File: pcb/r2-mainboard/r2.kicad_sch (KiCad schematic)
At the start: 0 parts

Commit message: R2: the six approved edits, and one of them was already done
Owner-approved 2026-08-19, KiCad closed for the pass.

1. R225 22k -> 20.5K/1%, LCSC C57105 (0402WGF2052TCE, UNI-ROYAL, the
   family the rest of the board already uses). Rendered and checked:
   R224 390k over R225 20.5k with R213 100k injecting VGH_DAC, so
   20.5||100 = 17.01k and VGH = 1.2 x (1 + 390/17.01) = 28.71 V at
   DAC = 0 -- exactly epd-port.md 10.3's target.
2. The five sense-divider caps that carried codes for the wrong
   capacitance -> C1523 (0402B102K500NT, 1 nF 50 V X7R, JLC Basic,
   5.3 M stock). One part covers both the 25 V and 50 V positions.
2b. R88/R224 -> C54920667 (HRC0402F3903DNTO, 390k 1%, 20 k stock).
   C25782 had 14 units against two per board. The owner found this one;
   both obvious alternatives were traps -- C23150 is 0603, and C44937
   is 3.9 ohm despite "390K" in its part number.
3. C147 set DNP rather than deleted. panel.md 7 had already ruled that
   J6.7/J6.44 stay; that covered the pins but not the capacitor on the
   dead net. DNP drops it from placement, keeps the topology of a frozen
   sheet untouched, and leaves the footprint if a future panel drives
   the rail. in_bom stays yes -- that is this board's convention for all
   13 DNP parts, so they show up flagged rather than vanishing.
4. Ten duplicate #PWR references renumbered to #PWR1112-1121 on the
   battery sheet, which was the colliding side in every case.
5. J3 was already deleted on 2026-08-15. No work needed.
6. Specter -> Reflow across 22 files: 14 sheets, 7 generators, the
   project file. .history/ deliberately untouched.

Verified as one change: netlist before and after has 518 nets with
identical pin membership, and epd_power and epd were rendered to PNG and
inspected.

Docs updated to match: epd-port.md 10 is applied rather than designed,
frontlight.md 1 loses the "9 in series is inferred" hedge (the vendor
listing confirms 2 x 9), and io-expansion.md 4's "only guess on this
sheet" is resolved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
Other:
- title: Glider-R2 / Specter mainboard -> Glider-R2 / Reflow mainboard
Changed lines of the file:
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@@
 	(paper "A3")
 	(title_block
-		(title "Glider-R2 / Specter mainboard")
+		(title "Glider-R2 / Reflow mainboard")
 		(date "2026-08-05")
 		(rev "A")

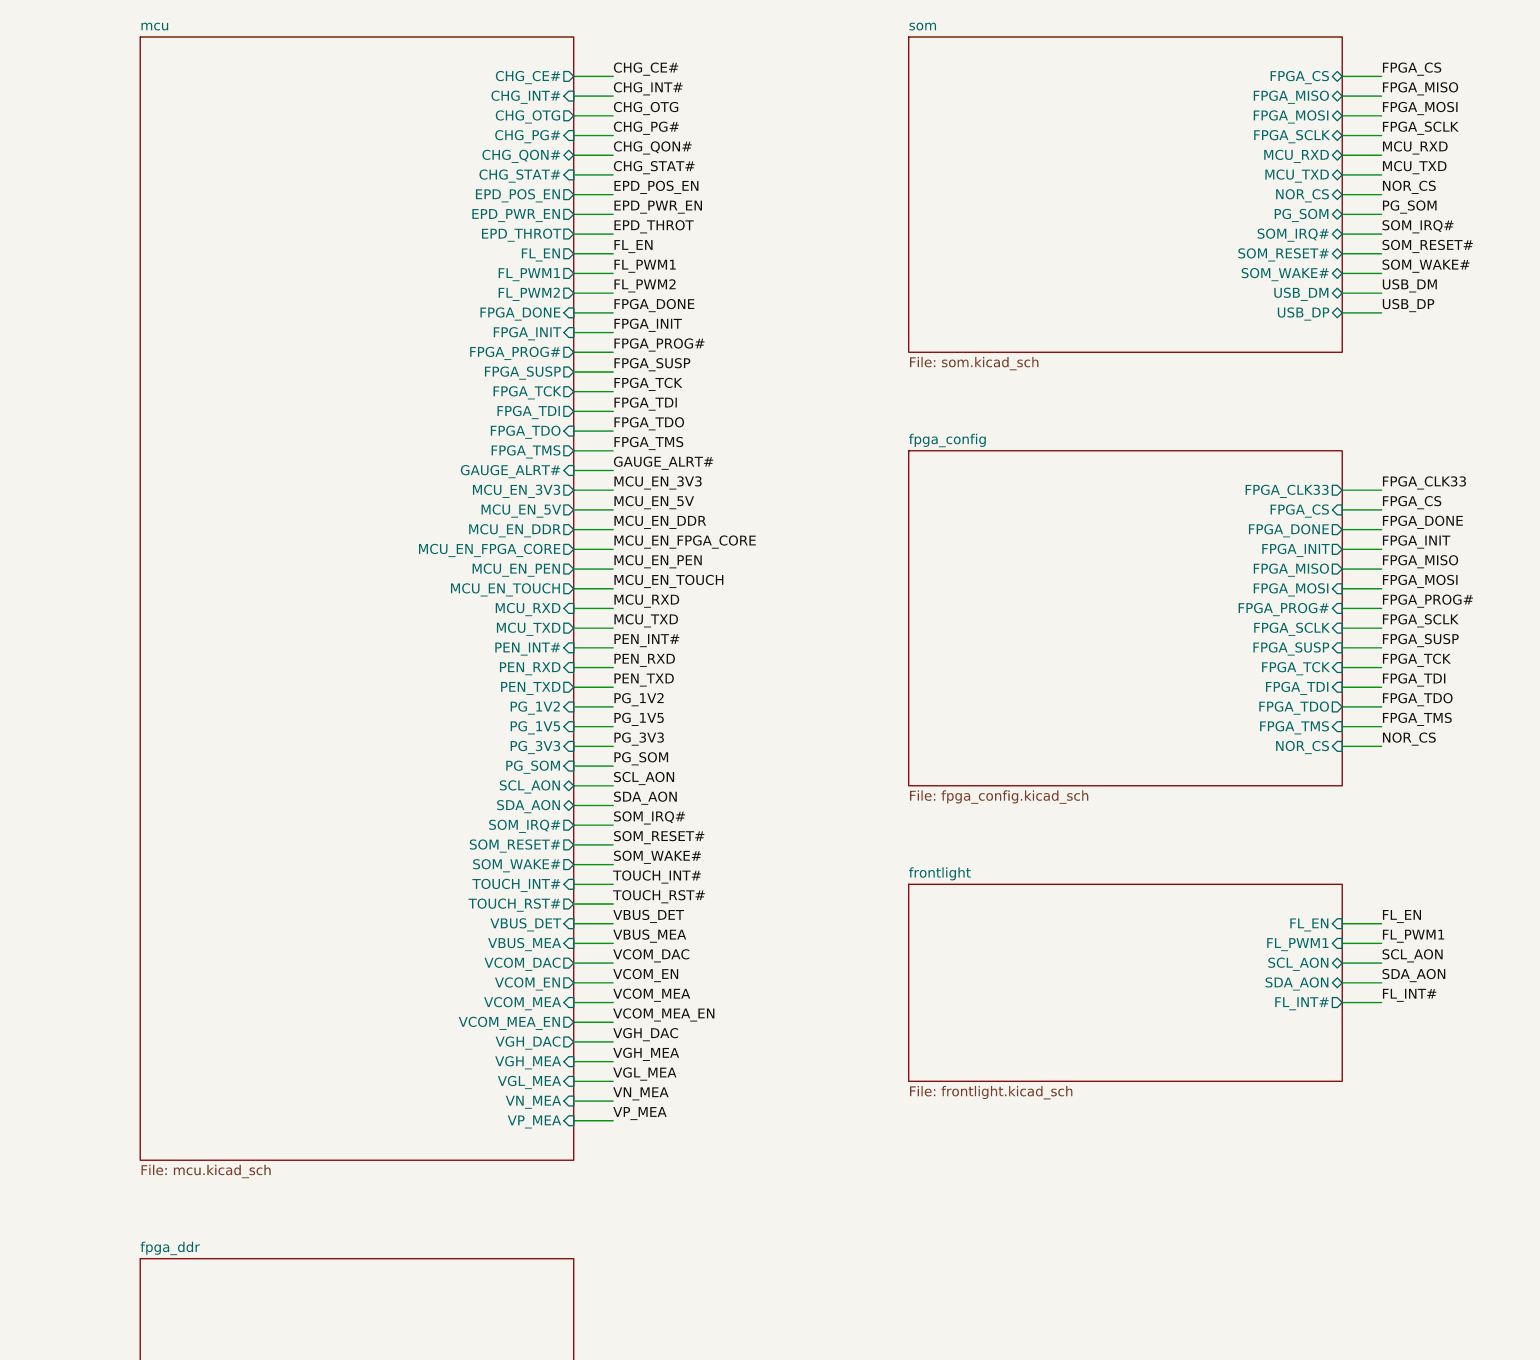
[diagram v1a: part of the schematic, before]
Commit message: R2: the SoM can now reset the MCU and force its bootloader (WP8 closed)
tools/patch_som_mcu_recovery.py applies mcu.md 5.8. On som, A59 and A60
lose their no-connects and gain SOM_MCU_NRST / SOM_MCU_BOOT0. On mcu,
three parts land on empty canvas at x>300:

  Q9    AO3400A  Transistor_FET:Q_NMOS_GSD, SOT-23, C347475
  R510  100k     gate pull-down
  R511  1k       series into PA14

NRST goes through the FET rather than straight to the pin, because the
MCU gates the SoM's own supply -- "SoM off, MCU alive" is the normal
standby state, and a direct tie would let an unpowered A59 clamp
MCU_NRST toward a dead VDDSHV_CANUART and hold the MCU in reset for
good. With Q9 the default is safe in every combination: gate low or SoM
unpowered leaves NRST to the STM32's internal pull-up.

BOOT0 needs no FET -- nothing on R2 drives PA14 high, so R40's pull-down
already defines the safe state, and R511 doubles as the contention limit
against an ST-LINK on the shared SWCLK pin.

Verified: 518 nets before and after; the only membership changes are
MCU_NRST += Q9.3, MCU_SWCLK += R511.2, GND += Q9.2/R510.2, plus the two
new nets and the two unconnected- entries that went away. Rendered to
PNG and inspected twice -- the first layout ran the MCU_NRST label
vertically into the BOOT0 row, so the drain now turns right first.

One trap recorded in mcu.md 5.8: set_sheet_pins re-lays every pin on a
root box, and the root's stubs and labels are positional, so adding two
pins silently rotated the membership of eighteen nets on the first run.
wire_root.py must be re-run after any sheet-pin change; the patch script
now does that itself and asserts on its exit code.

RM0444 (now in datasheets/) settles the factory question from source:
3.3.1 p.67, the EMPTY flag "allows easy programming of virgin devices by
the boot loader", so a blank board needs only an SD card. Riders: the
first flash needs a power cycle or OBL_LAUNCH to reload option bytes,
and the BOOT0 pin still earns its keep for recovery, w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
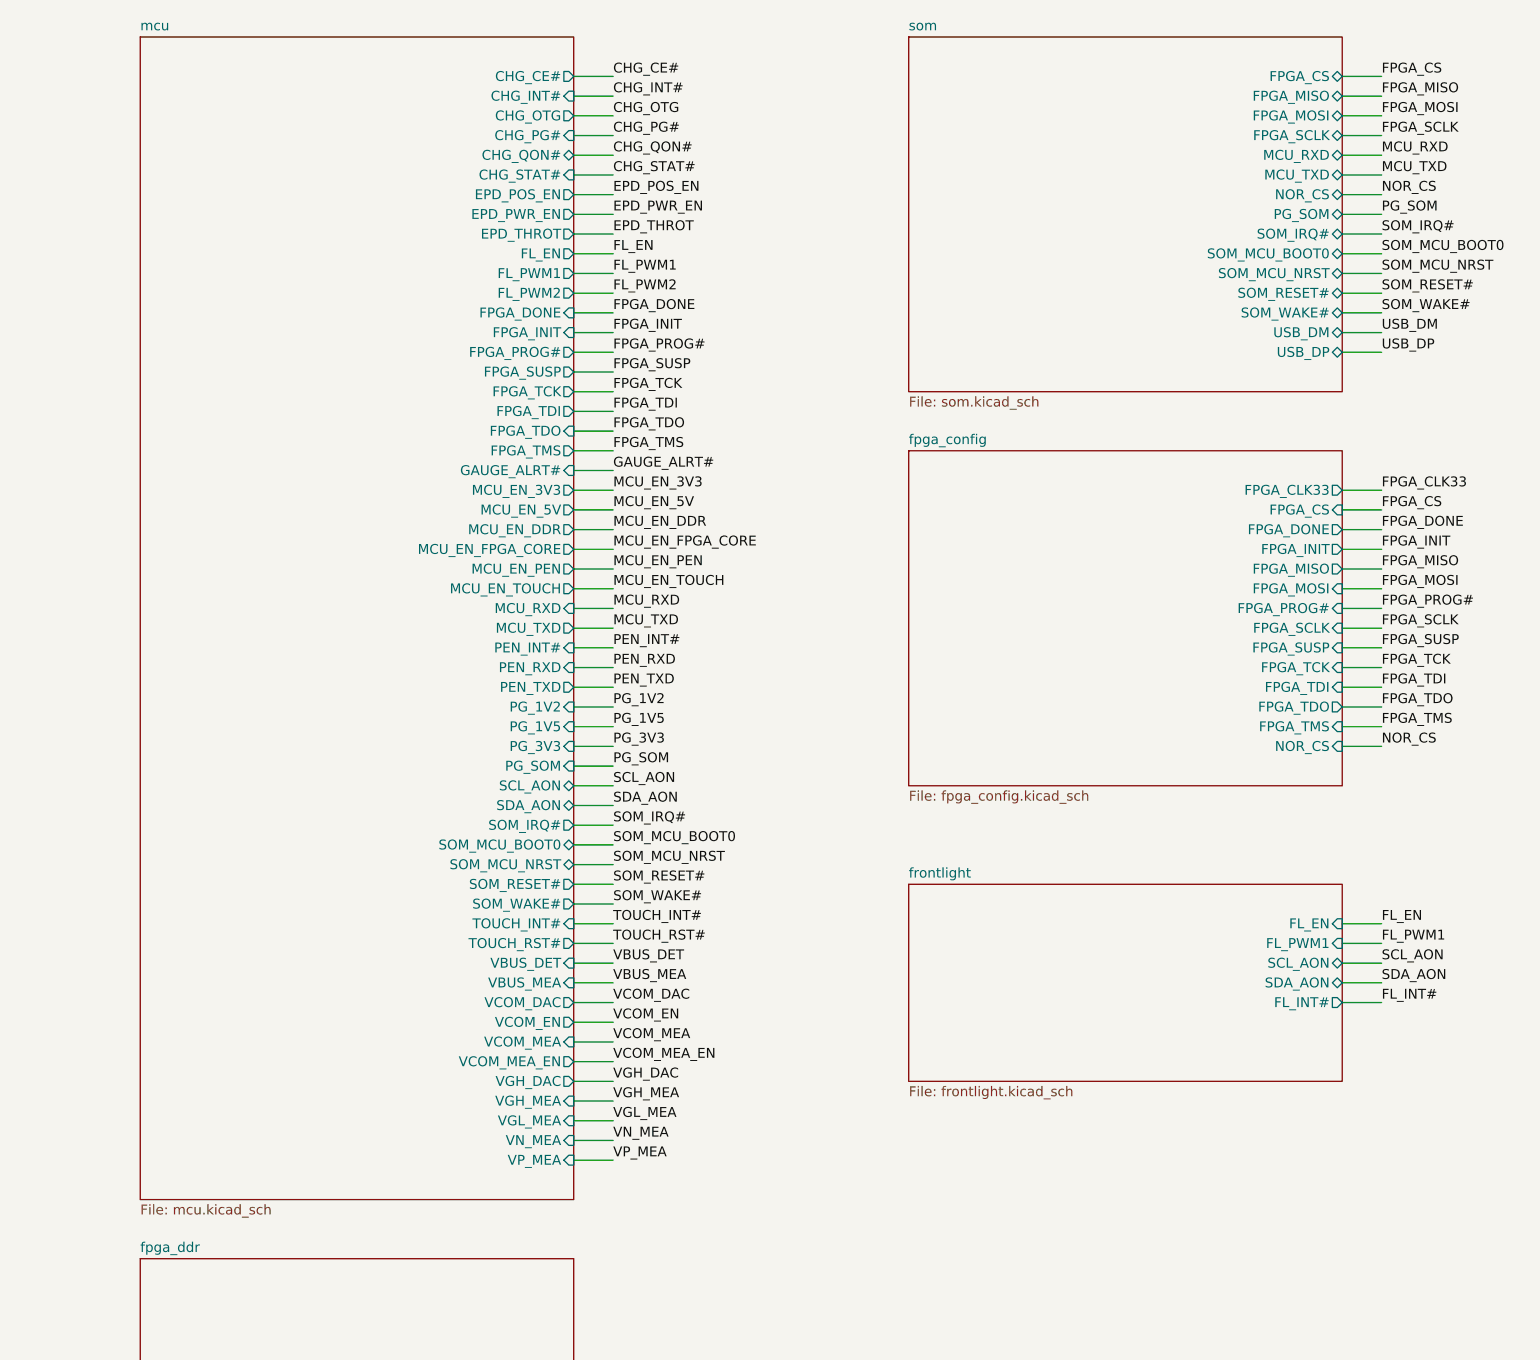
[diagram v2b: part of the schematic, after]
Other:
- sheet mcu ports: added SOM_MCU_BOOT0, SOM_MCU_NRST; removed none
- sheet som ports: added SOM_MCU_BOOT0, SOM_MCU_NRST; removed none

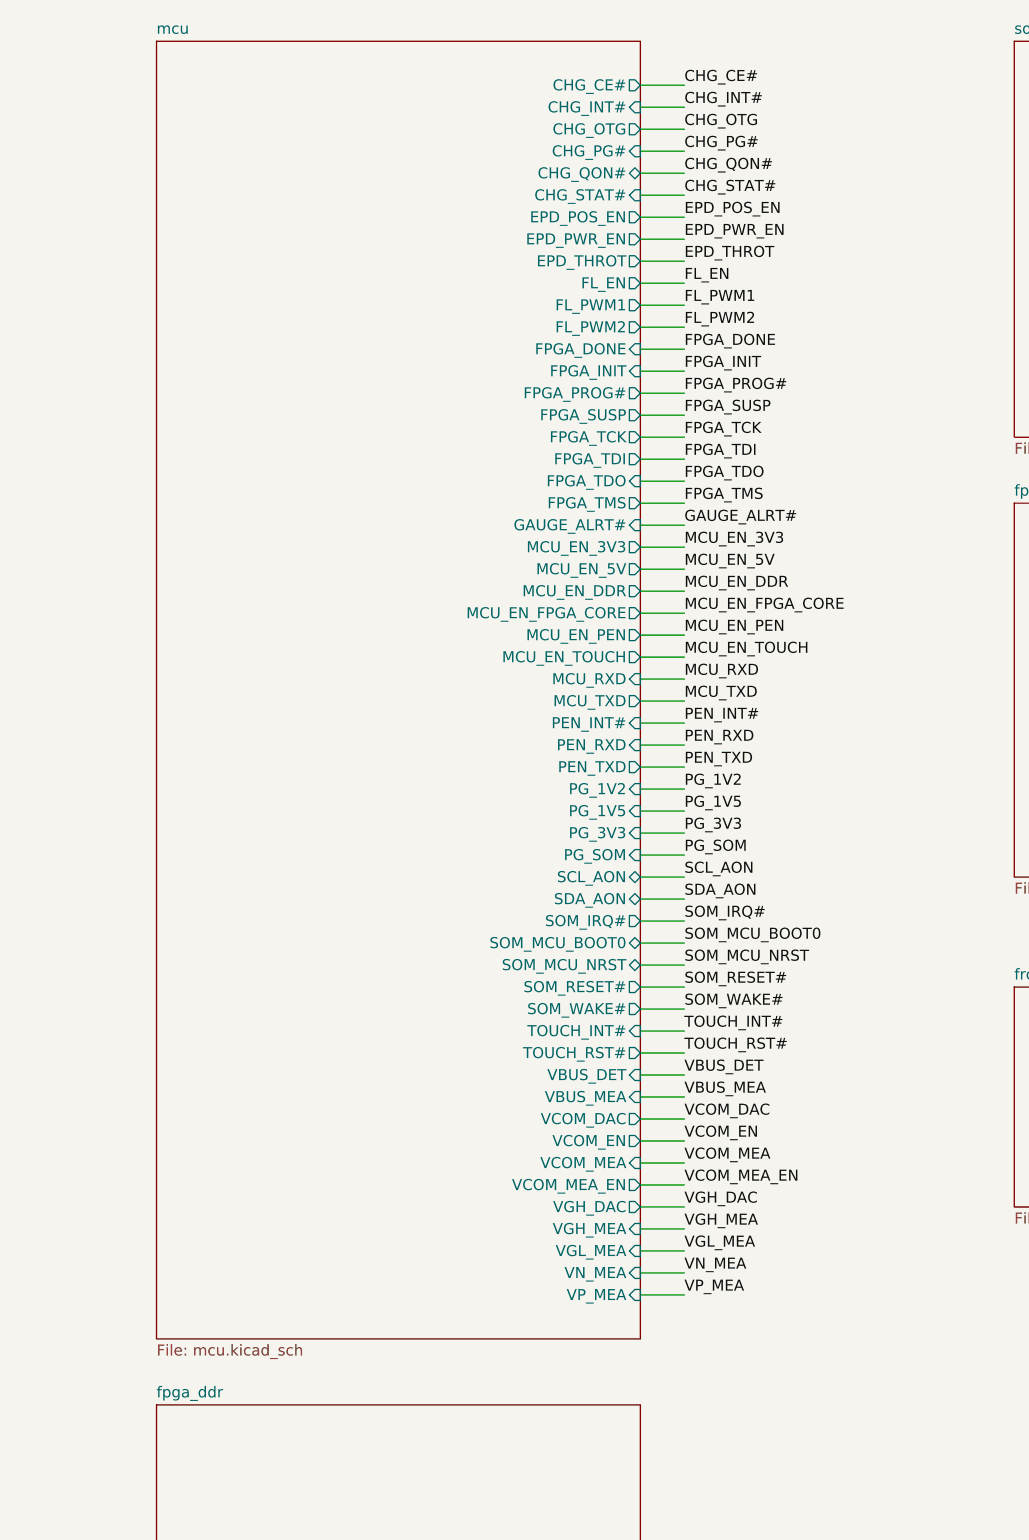
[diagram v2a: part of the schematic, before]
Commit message: R2: two interrupts that could never fire, and the SoM footprint
The EXTI collisions mcu.md §3.4 found are applied. An EXTI line is picked
by the pin's *number*, so TOUCH_INT# on PC3 was fighting PD3 GAUGE_ALRT#
and PEN_INT# on PC6 was fighting PD6 QON_SNS -- as drawn neither touch nor
pen could raise an interrupt at all. Each swaps with an output, which needs
no line, so it costs nothing. FL_INT# gets PB12 at the same time, which was
frontlight.md §10.3's own first suggestion; §9's later push for PB7 was
wrong, because PC7 KEY_PREV# holds EXTI7.

518 -> 517 nets, the drop being the PB12 unconnected- pseudo-net, and
exactly five membership changes. Every hierarchical label in the project
now has a counterpart -- DANGLING_OK is empty and ERC excluding
footprint_link_issues is 32, down from 105.

The PCM-071 footprint is built rather than downloaded, because two drawings
have landed that over-determine it: Samtec's own vector land pattern (parsed
from the content stream, every measurement agreeing with a printed dimension
to under 1 um) and L-1038e.A5 Figure 7, which is a carrier-board drawing.
The trap it contains is that the alignment hole is NOT on the connector's
centreline -- it is 1.054 mm from one row and 5.118 from the other, and
Figure 7 dimensions the holes, so assuming a centred hole puts both
connectors 2.06 mm out. The check worth trusting is the one nothing forces:
the B and C rows land 0.982 and 0.998 mm inside the module's edges.

Also: U41's speed grade is settled -2 -- LCSC has no -3 in FTG256 at all,
and caster.xise's -3 is ISE's untouched default (valueState="default"), not
a choice anyone made. But -2's MCB is rated 667 Mb/s against the 666.67 this
design runs, so fpga.md §1.1 asks for one free ISE build before the order.

And a bring-up landmine: epd_pos_rails_good() accepts VGH <= 28.0 V while
R2's own R225 change puts it at 28.41 V nominal. A correctly built board
would fatal() at every EPD power-up. epd-port.md §10.5.

Co-Authored-By: Claude Op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
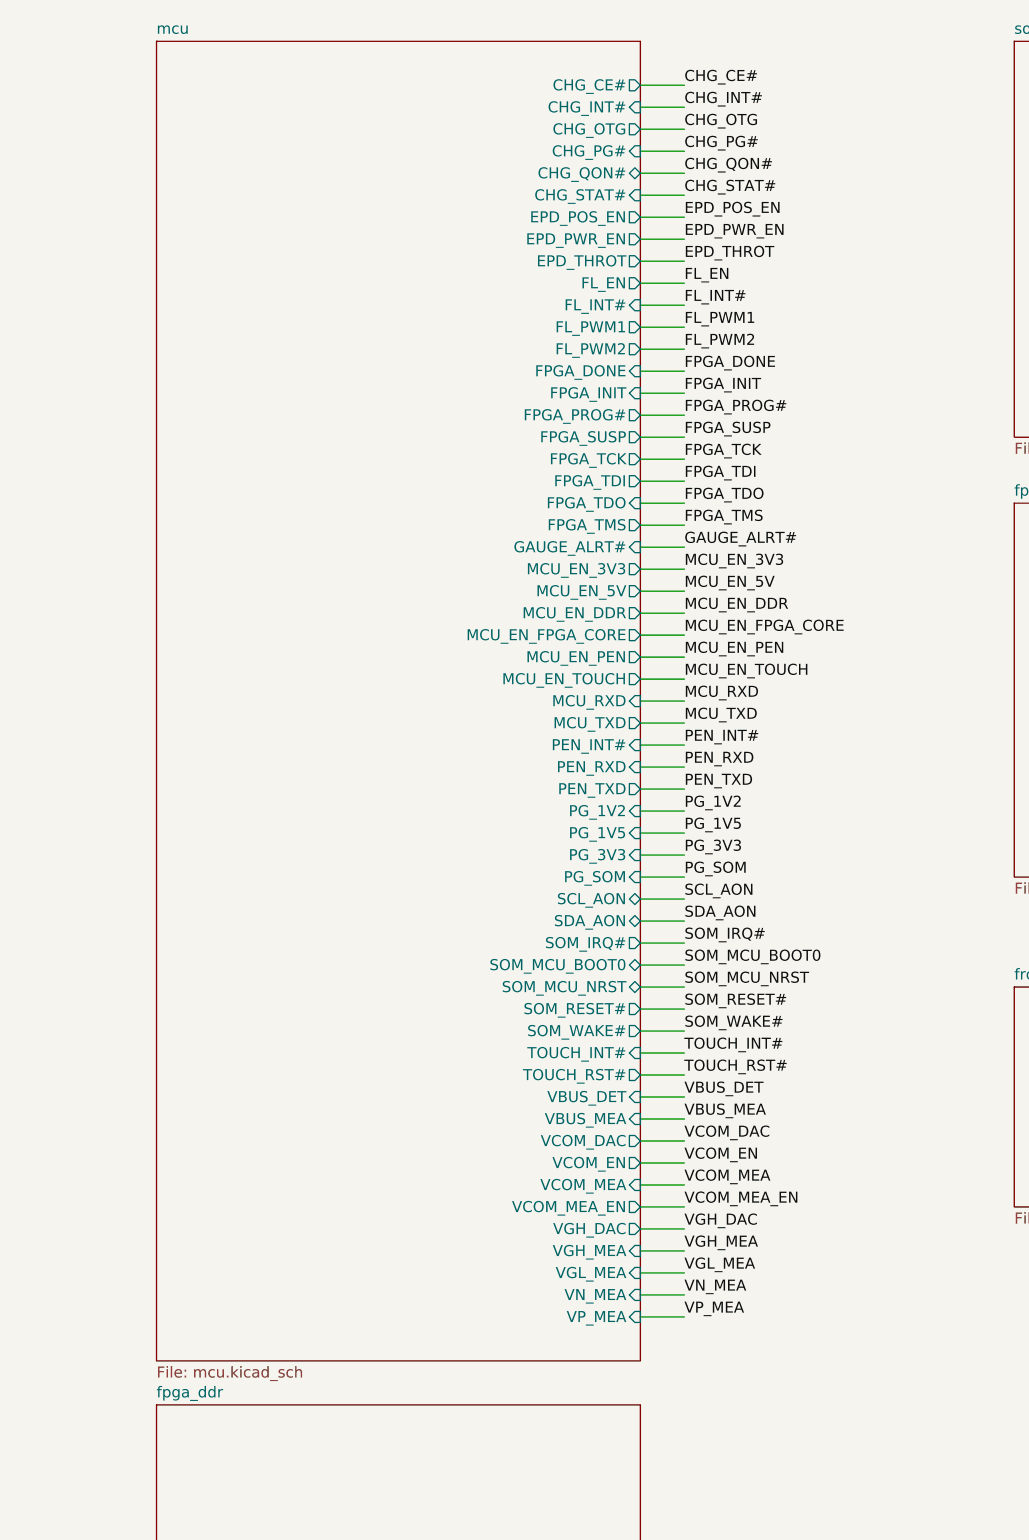
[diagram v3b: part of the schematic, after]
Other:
- sheet mcu ports: added FL_INT#; removed none
